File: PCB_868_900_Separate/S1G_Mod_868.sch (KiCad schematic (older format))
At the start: 56 parts, among them Q1 DMG2307L-7, SW1 CUS-12TB, T1 0732511150, T2 0732511150, U1 AP7361-33FGE-7, U2 ADF7023BCPZ, X1 ABS05-32.768KHZ-9-T, X2 ABM11-140-26.000MHZ-T3

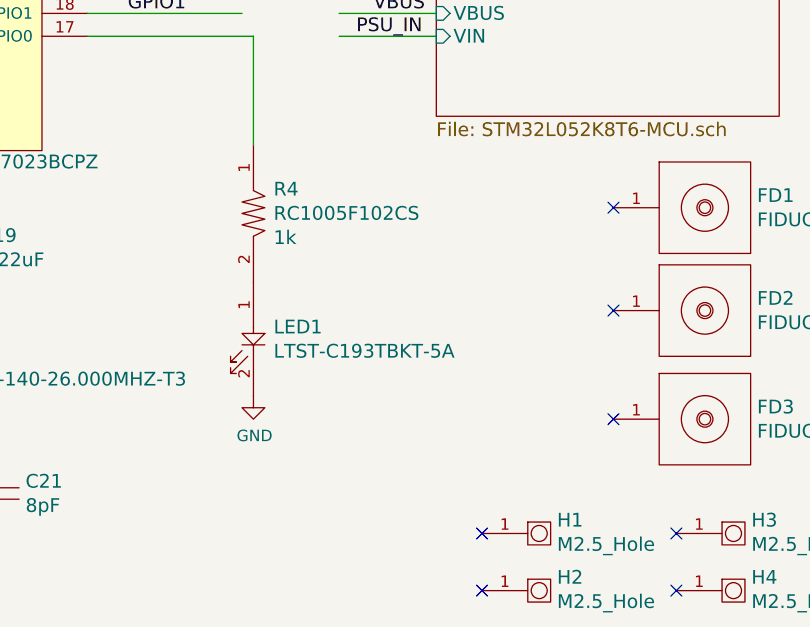
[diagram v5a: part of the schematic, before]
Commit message: More LDO
LDO section on separate antenna version retooled to be more like the
combined antenna version. Added additional fudicials on the bottom.
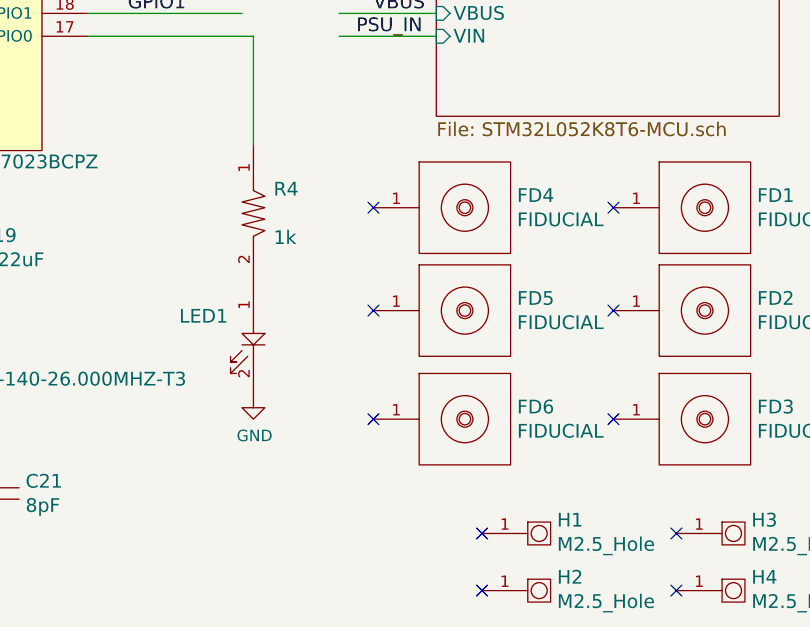
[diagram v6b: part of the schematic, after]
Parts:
- added FD4, FD5, FD6: FIDUCIAL, PCB_Footprints:FIDUCIAL, symbol FIDUCIAL
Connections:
- no-connect marks 12 -> 15
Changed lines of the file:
@@
 $EndComp
 $Comp
-L GND #PWR01
+L GND #PWR26
 U 1 1 58161058
 P 7000 6125
-F 0 "#PWR01" H 7000 5875 50  0001 C CNN
+F 0 "#PWR26" H 7000 5875 50  0001 C CNN
 F 1 "GND" H 7005 5952 50  0000 C CNN
 F 2 "" H 7000 6125 50  0000 C CNN
@@
 $EndComp
 $Comp
-L GND #PWR02
+L GND #PWR18
 U 1 1 5816222C
 P 5850 4375
-F 0 "#PWR02" H 5850 4125 50  0001 C CNN
+F 0 "#PWR18" H 5850 4125 50  0001 C CNN
 F 1 "GND" H 5855 4202 50  0000 C CNN
 F 2 "" H 5850 4375 50  0000 C CNN
@@
 $EndComp
 $Comp
-L +3.3V #PWR03
+L +3.3V #PWR17
 U 1 1 581623E1
 P 5400 2125
-F 0 "#PWR03" H 5400 1975 50  0001 C CNN
+F 0 "#PWR17" H 5400 1975 50  0001 C CNN
 F 1 "+3.3V" H 5415 2298 50  0000 C CNN
 F 2 "" H 5400 2125 50  0000 C CNN
@@
 $EndComp
 $Comp
-L GND #PWR04
+L GND #PWR15
 U 1 1 58162F98
 P 4950 3300
-F 0 "#PWR04" H 4950 3050 50  0001 C CNN
+F 0 "#PWR15" H 4950 3050 50  0001 C CNN
 F 1 "GND" H 4955 3127 50  0000 C CNN
 F 2 "" H 4950 3300 50  0000 C CNN
@@
 $EndComp
 $Comp
-L GND #PWR05
+L GND #PWR24
 U 1 1 58164E94
 P 6200 5050
-F 0 "#PWR05" H 6200 4800 50  0001 C CNN
+F 0 "#PWR24" H 6200 4800 50  0001 C CNN
 F 1 "GND" H 6205 4877 50  0000 C CNN
 F 2 "" H 6200 5050 50  0000 C CNN
@@
 $EndComp
 $Comp
-L GND #PWR06
+L GND #PWR27
 U 1 1 58165059
 P 7250 5050
-F 0 "#PWR06" H 7250 4800 50  0001 C CNN
+F 0 "#PWR27" H 7250 4800 50  0001 C CNN
 F 1 "GND" H 7255 4877 50  0000 C CNN
 F 2 "" H 7250 5050 50  0000 C CNN
@@
 $EndComp
 $Comp
-L GND #PWR07
+L GND #PWR25
 U 1 1 58165567
 P 6850 5050
-F 0 "#PWR07" H 6850 4800 50  0001 C CNN
+F 0 "#PWR25" H 6850 4800 50  0001 C CNN
 F 1 "GND" H 6855 4877 50  0000 C CNN
 F 2 "" H 6850 5050 50  0000 C CNN
@@
 U 1 1 58168200
 P 8575 5225
-F 0 "LED1" V 8522 5313 60  0000 L CNN
-F 1 "LTST-C193TBKT-5A" V 8628 5313 60  0000 L CNN
+F 0 "LED1" V 8475 4900 60  0000 L CNN
+F 1 "LTST-C193TBKT-5A" V 8628 5313 60  0001 L CNN
 F 2 "PCB_Footprints:LED0603" H 10000 7150 60  0001 C CNN
 F 3 "http://optoelectronics.liteon.com/upload/download/DS22-2004-060/P_100_LTST-C193TBKT-5A.pdf" H 10200 7275 60  0001 C CNN
@@
 $EndComp
 $Comp
-L GND #PWR08
+L GND #PWR31
 U 1 1 58168376
 P 8575 5475
-F 0 "#PWR08" H 8575 5225 50  0001 C CNN
+F 0 "#PWR31" H 8575 5225 50  0001 C CNN
 F 1 "GND" H 8580 5302 50  0000 C CNN
 F 2 "" H 8575 5475 50  0000 C CNN
@@
 $EndComp
 $Comp
-L +3.3V #PWR09
+L +3.3V #PWR19
 U 1 1 58168986
 P 5875 1325
-F 0 "#PWR09" H 5875 1175 50  0001 C CNN
+F 0 "#PWR19" H 5875 1175 50  0001 C CNN
 F 1 "+3.3V" H 5890 1498 50  0000 C CNN
 F 2 "" H 5875 1325 50  0000 C CNN
@@
 $EndComp
 $Comp
-L GND #PWR010
+L GND #PWR14
 U 1 1 58169314
 P 4950 2350
-F 0 "#PWR010" H 4950 2100 50  0001 C CNN
+F 0 "#PWR14" H 4950 2100 50  0001 C CNN
 F 1 "GND" H 4955 2177 50  0000 C CNN
 F 2 "" H 4950 2350 50  0000 C CNN
@@
 $EndComp
 $Comp
-L GND #PWR011
+L GND #PWR2
 U 1 1 5817FFB1
 P 725 4875
-F 0 "#PWR011" H 725 4625 50  0001 C CNN
+F 0 "#PWR2" H 725 4625 50  0001 C CNN
 F 1 "GND" H 730 4702 50  0000 C CNN
 F 2 "" H 725 4875 50  0000 C CNN
@@
 $EndComp
 $Comp
-L GND #PWR012
+L GND #PWR3
 U 1 1 58174222
 P 2000 5050
-F 0 "#PWR012" H 2000 4800 50  0001 C CNN
+F 0 "#PWR3" H 2000 4800 50  0001 C CNN
 F 1 "GND" H 2005 4877 50  0000 C CNN
 F 2 "" H 2000 5050 50  0000 C CNN
@@
 $EndComp
 $Comp
-L GND #PWR013
+L GND #PWR5
 U 1 1 581744A7
 P 2800 5050
-F 0 "#PWR013" H 2800 4800 50  0001 C CNN
+F 0 "#PWR5" H 2800 4800 50  0001 C CNN
 F 1 "GND" H 2805 4877 50  0000 C CNN
 F 2 "" H 2800 5050 50  0000 C CNN
@@
 $EndComp
 $Comp
-L GND #PWR014
+L GND #PWR11
 U 1 1 5816BC64
 P 4000 6500
-F 0 "#PWR014" H 4000 6250 50  0001 C CNN
+F 0 "#PWR11" H 4000 6250 50  0001 C CNN
 F 1 "GND" H 4005 6327 50  0000 C CNN
 F 2 "" H 4000 6500 50  0000 C CNN
@@
 $EndComp
 $Comp
-L GND #PWR015
+L GND #PWR21
 U 1 1 5816BFC1
 P 5875 6500
-F 0 "#PWR015" H 5875 6250 50  0001 C CNN
+F 0 "#PWR21" H 5875 6250 50  0001 C CNN
 F 1 "GND" H 5880 6327 50  0000 C CNN
 F 2 "" H 5875 6500 50  0000 C CNN
@@
 $EndComp
 $Comp
-L +3.3V #PWR016
+L +3.3V #PWR20
 U 1 1 5816C55D
 P 5875 6050
-F 0 "#PWR016" H 5875 5900 50  0001 C CNN
+F 0 "#PWR20" H 5875 5900 50  0001 C CNN
 F 1 "+3.3V" H 5890 6223 50  0000 C CNN
 F 2 "" H 5875 6050 50  0000 C CNN
@@
 MCU_IRQ
 $Comp
-L GND #PWR017
+L GND #PWR23
 U 1 1 58175F58
 P 6175 1825
-F 0 "#PWR017" H 6175 1575 50  0001 C CNN
+F 0 "#PWR23" H 6175 1575 50  0001 C CNN
 F 1 "GND" H 6180 1652 50  0000 C CNN
 F 2 "" H 6175 1825 50  0000 C CNN
@@
 $EndComp
 $Comp
-L GND #PWR018
+L GND #PWR28
 U 1 1 581763CA
 P 7675 1825
-F 0 "#PWR018" H 7675 1575 50  0001 C CNN
+F 0 "#PWR28" H 7675 1575 50  0001 C CNN
 F 1 "GND" H 7680 1652 50  0000 C CNN
 F 2 "" H 7675 1825 50  0000 C CNN
@@
 $EndComp
 $Comp
-L GND #PWR019
+L GND #PWR9
 U 1 1 5817CEBD
 P 3650 2200
-F 0 "#PWR019" H 3650 1950 50  0001 C CNN
+F 0 "#PWR9" H 3650 1950 50  0001 C CNN
 F 1 "GND" H 3655 2027 50  0000 C CNN
 F 2 "" H 3650 2200 50  0000 C CNN
@@
 $EndComp
 $Comp
-L GND #PWR020
+L GND #PWR13
 U 1 1 5817CF2D
 P 4450 2200
-F 0 "#PWR020" H 4450 1950 50  0001 C CNN
+F 0 "#PWR13" H 4450 1950 50  0001 C CNN
 F 1 "GND" H 4455 2027 50  0000 C CNN
 F 2 "" H 4450 2200 50  0000 C CNN
@@
 $EndComp
 $Comp
-L +3.3V #PWR021
+L +3.3V #PWR6
 U 1 1 5817CF98
 P 3150 1750
-F 0 "#PWR021" H 3150 1600 50  0001 C CNN
+F 0 "#PWR6" H 3150 1600 50  0001 C CNN
 F 1 "+3.3V" H 3165 1923 50  0000 C CNN
 F 2 "" H 3150 1750 50  0000 C CNN
@@
 $EndComp
 $Comp
-L GND #PWR022
+L GND #PWR8
 U 1 1 5818E84F
 P 3600 5050
-F 0 "#PWR022" H 3600 4800 50  0001 C CNN
+F 0 "#PWR8" H 3600 4800 50  0001 C CNN
 F 1 "GND" H 3605 4877 50  0000 C CNN
 F 2 "" H 3600 5050 50  0000 C CNN
@@
 $EndComp
 $Comp
-L GND #PWR023
+L GND #PWR10
 U 1 1 58195E9E
 P 3675 4100
-F 0 "#PWR023" H 3675 3850 50  0001 C CNN
+F 0 "#PWR10" H 3675 3850 50  0001 C CNN
 F 1 "GND" H 3680 3927 50  0000 C CNN
 F 2 "" H 3675 4100 50  0000 C CNN
@@
 $EndComp
 $Comp
-L GND #PWR024
+L GND #PWR4
 U 1 1 58196935
 P 2800 3025
-F 0 "#PWR024" H 2800 2775 50  0001 C CNN
+F 0 "#PWR4" H 2800 2775 50  0001 C CNN
 F 1 "GND" H 2805 2852 50  0000 C CNN
 F 2 "" H 2800 3025 50  0000 C CNN
@@
 $EndComp
 $Comp
-L GND #PWR025
+L GND #PWR1
 U 1 1 581979F7
 P 700 3650
-F 0 "#PWR025" H 700 3400 50  0001 C CNN
+F 0 "#PWR1" H 700 3400 50  0001 C CNN
 F 1 "GND" H 705 3477 50  0000 C CNN
 F 2 "" H 700 3650 50  0000 C CNN
@@
 $EndComp
 $Comp
-L +3.3V #PWR026
+L +3.3V #PWR29
 U 1 1 581AA58C
 P 8350 2600
-F 0 "#PWR026" H 8350 2450 50  0001 C CNN
+F 0 "#PWR29" H 8350 2450 50  0001 C CNN
 F 1 "+3.3V" H 8365 2773 50  0000 C CNN
 F 2 "" H 8350 2600 50  0000 C CNN
@@
 	6175 7300 6450 7300
 $Comp
-L GND #PWR027
+L GND #PWR22
 U 1 1 5822EA21
 P 6050 7125
-F 0 "#PWR027" H 6050 6875 50  0001 C CNN
+F 0 "#PWR22" H 6050 6875 50  0001 C CNN
 F 1 "GND" H 6055 6952 50  0000 C CNN
 F 2 "" H 6050 7125 50  0000 C CNN
@@
 $EndComp
 $Comp
-L GND #PWR028
+L GND #PWR12
 U 1 1 5825B89E
 P 4150 5250
-F 0 "#PWR028" H 4150 5000 50  0001 C CNN
+F 0 "#PWR12" H 4150 5000 50  0001 C CNN
 F 1 "GND" H 4155 5077 50  0000 C CNN
 F 2 "" H 4150 5250 50  0000 C CNN
@@
 $EndComp
 $Comp
-L GND #PWR029
+L GND #PWR16
 U 1 1 582688A4
 P 4950 7350
-F 0 "#PWR029" H 4950 7100 50  0001 C CNN
+F 0 "#PWR16" H 4950 7100 50  0001 C CNN
 F 1 "GND" H 4955 7177 50  0000 C CNN
 F 2 "" H 4950 7350 50  0000 C CNN
@@
 	3850 7350 3425 7350
 $Comp
-L +3.3V #PWR030
+L +3.3V #PWR7
 U 1 1 582692EE
 P 3425 7350
-F 0 "#PWR030" H 3425 7200 50  0001 C CNN
+F 0 "#PWR7" H 3425 7200 50  0001 C CNN
 F 1 "+3.3V" H 3440 7523 50  0000 C CNN
 F 2 "" H 3425 7350 50  0000 C CNN
@@
 P 8575 4675
 F 0 "R4" V 8469 4763 60  0000 L CNN
-F 1 "RC1005F102CS" V 8575 4763 60  0000 L CNN
+F 1 "RC1005F102CS" V 8600 4850 60  0001 L CNN
 F 2 "PCB_Footprints:R0402" H 8175 4925 60  0001 C CNN
 F 3 "https://media.digikey.com/pdf/Data%20Sheets/Samsung%20PDFs/RC_Series_ds.pdf" H 8275 5125 60  0001 C CNN
@@
 	7100 2100 7100 2550
 $Comp
-L GND #PWR031
+L GND #PWR30
 U 1 1 582AF362
 P 8425 2100
-F 0 "#PWR031" H 8425 1850 50  0001 C CNN
+F 0 "#PWR30" H 8425 1850 50  0001 C CNN
 F 1 "GND" H 8430 1927 50  0000 C CNN
 F 2 "" H 8425 2100 50  0000 C CNN
@@
 	1    0    0    -1
 $EndComp
+$Comp
+L FIDUCIAL FD4
+U 1 1 582BCD13
+P 9300 4650
+F 0 "FD4" H 9728 4703 60  0000 L CNN
+F 1 "FIDUCIAL" H 9728 4597 60  0000 L CNN
+F 2 "PCB_Footprints:FIDUCIAL" H 9775 5250 197 0001 C CNN
+F 3 "" H 9300 4650 197 0001 C CNN
+	1    9300 4650
+	1    0    0    -1
+$EndComp
+$Comp
+L FIDUCIAL FD5
+U 1 1 582BCD19
+P 9300 5100
+F 0 "FD5" H 9728 5153 60  0000 L CNN
+F 1 "FIDUCIAL" H 9728 5047 60  0000 L CNN
+F 2 "PCB_Footprints:FIDUCIAL" H 9775 5700 197 0001 C CNN
+F 3 "" H 9300 5100 197 0001 C CNN
+	1    9300 5100
+	1    0    0    -1
+$EndComp
+$Comp
+L FIDUCIAL FD6
+U 1 1 582BCD1F
+P 9300 5575
+F 0 "FD6" H 9728 5628 60  0000 L CNN
+F 1 "FIDUCIAL" H 9728 5522 60  0000 L CNN
+F 2 "PCB_Footprints:FIDUCIAL" H 9775 6175 197 0001 C CNN
+F 3 "" H 9300 5575 197 0001 C CNN
+	1    9300 5575
+	1    0    0    -1
+$EndComp
+NoConn ~ 9100 4650
+NoConn ~ 9100 5100
+NoConn ~ 9100 5575
 $EndSCHEMATC
